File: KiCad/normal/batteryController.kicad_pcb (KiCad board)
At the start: 2 copper layers, 55.5 x 36 mm, 20 parts, among them J1 Screw_Terminal_01x02, J2 Conn_01x04_Male, J3 Conn_01x04_Male, J4 Conn_01x04_Male, J5 Conn_02x04_Odd_Even, J6 Conn_01x01_Male, J7 USB_A, U1 ATtiny45V-10P, U2 LM2596S-ADJ, U3 LP2950-3.3_TO92

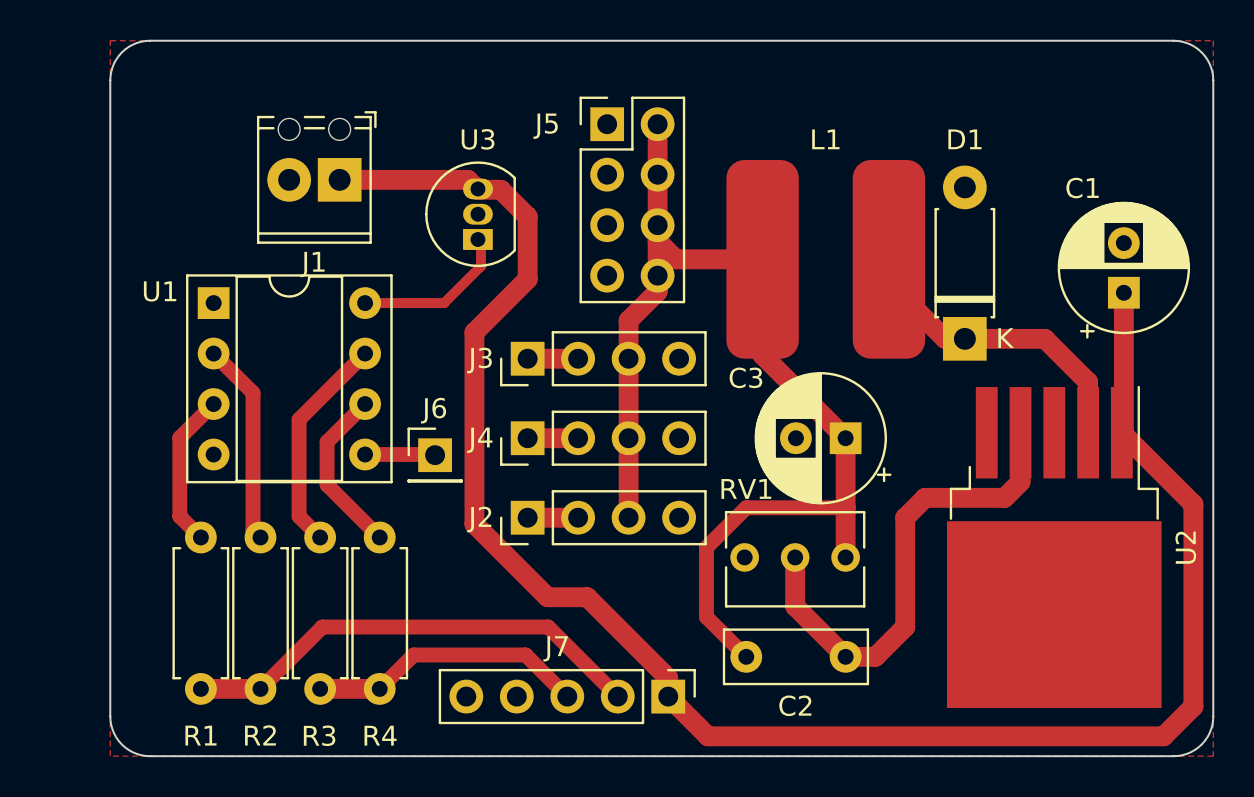
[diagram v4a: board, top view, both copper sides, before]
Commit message: spaced even further out for pcb milling
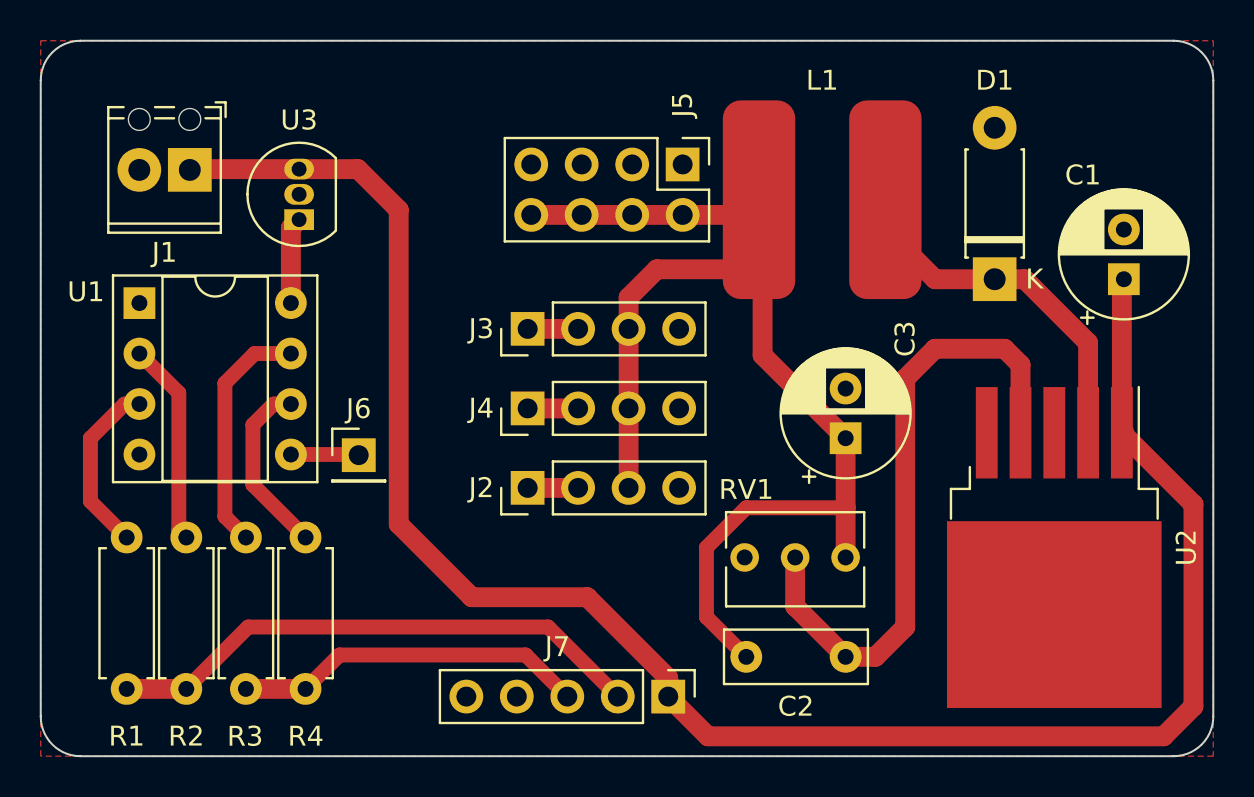
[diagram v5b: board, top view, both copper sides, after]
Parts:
- moved U3 9.06 mm to (57.5, 59.0)
- moved J1 7.56 mm to (52.0, 56.5)
- moved J5 4.31 mm to (76.8, 56.2), turned to -90 degrees
- moved J6 3.84 mm to (60.5, 70.9)
- moved R1 3.73 mm to (48.8, 75.0)
- moved R2 3.73 mm to (51.8, 75.0)
- moved R3 3.73 mm to (54.8, 75.0)
- moved R4 3.73 mm to (57.8, 75.0)
- moved U1 3.73 mm to (49.5, 63.2)
- moved D1 3.35 mm to (92.5, 62.0)
- moved L1 3.01 mm to (83.8, 58.0)
- moved J2 1.50 mm to (69.0, 72.5)
- moved J3 1.50 mm to (69.0, 64.5)
- moved J4 1.50 mm to (69.0, 68.5)
- moved C1 0.68 mm to (99.0, 62.0)
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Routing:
- net /FB: track 24.2 -> 32.4 mm
- net /VBUS: track 90.9 -> 95.9 mm
- net /OUT: track 56.2 -> 61.1 mm
- net Net-(R1-Pad2): track 23.7 -> 27.5 mm
- net Net-(J7-Pad3): track 14.0 -> 17.7 mm
- net /5V: track 7.45 -> 4.37 mm
- net /ROUT: track 17.5 -> 19.8 mm
- net Net-(R1-Pad1): track 7.86 -> 8.93 mm
- net Net-(R3-Pad1): track 11.1 -> 12.1 mm
- net Net-(R4-Pad1): track 8.60 -> 9.11 mm
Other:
- board size 55.5 x 36 mm -> 59 x 36 mm
